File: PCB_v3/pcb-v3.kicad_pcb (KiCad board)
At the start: 2 copper layers, 6 parts, among them J1 Conn_02x20_Odd_Even, J2 Conn_01x07_Socket, J4 Screw_Terminal_01x02

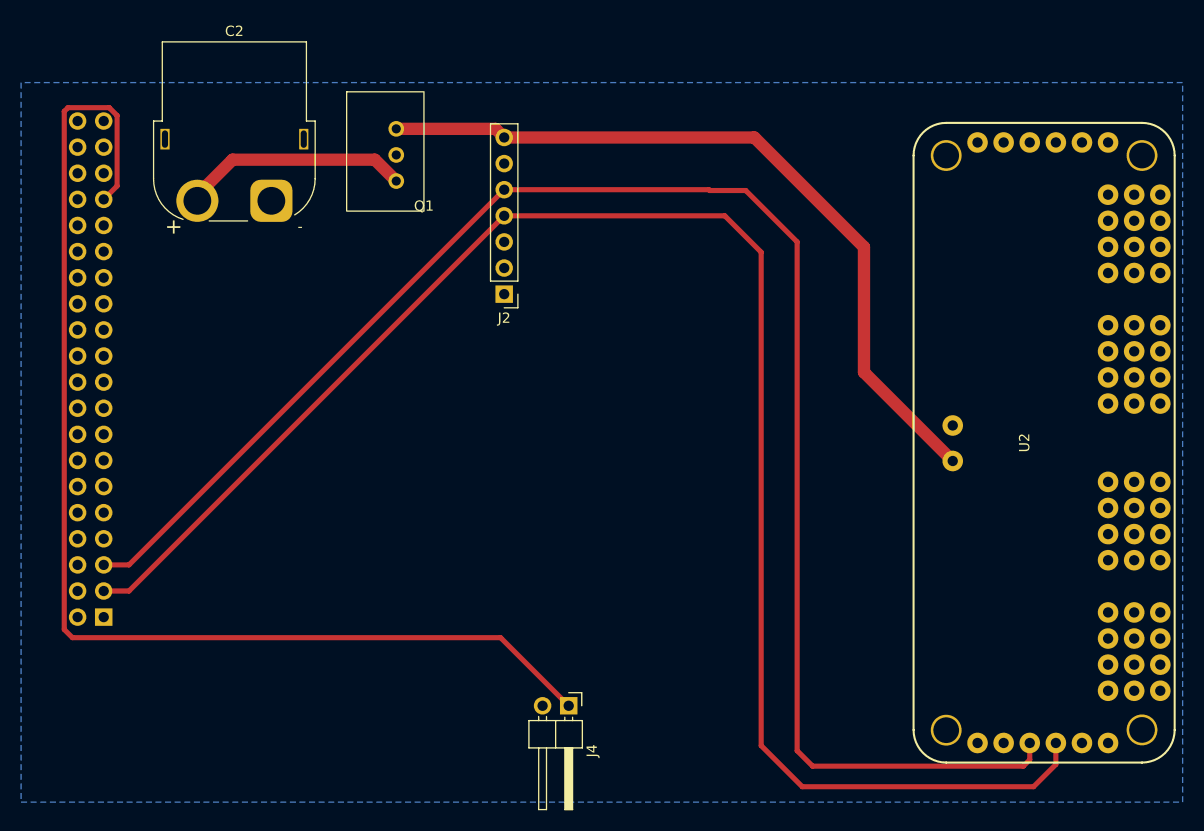
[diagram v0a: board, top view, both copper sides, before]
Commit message: completed board with labels included
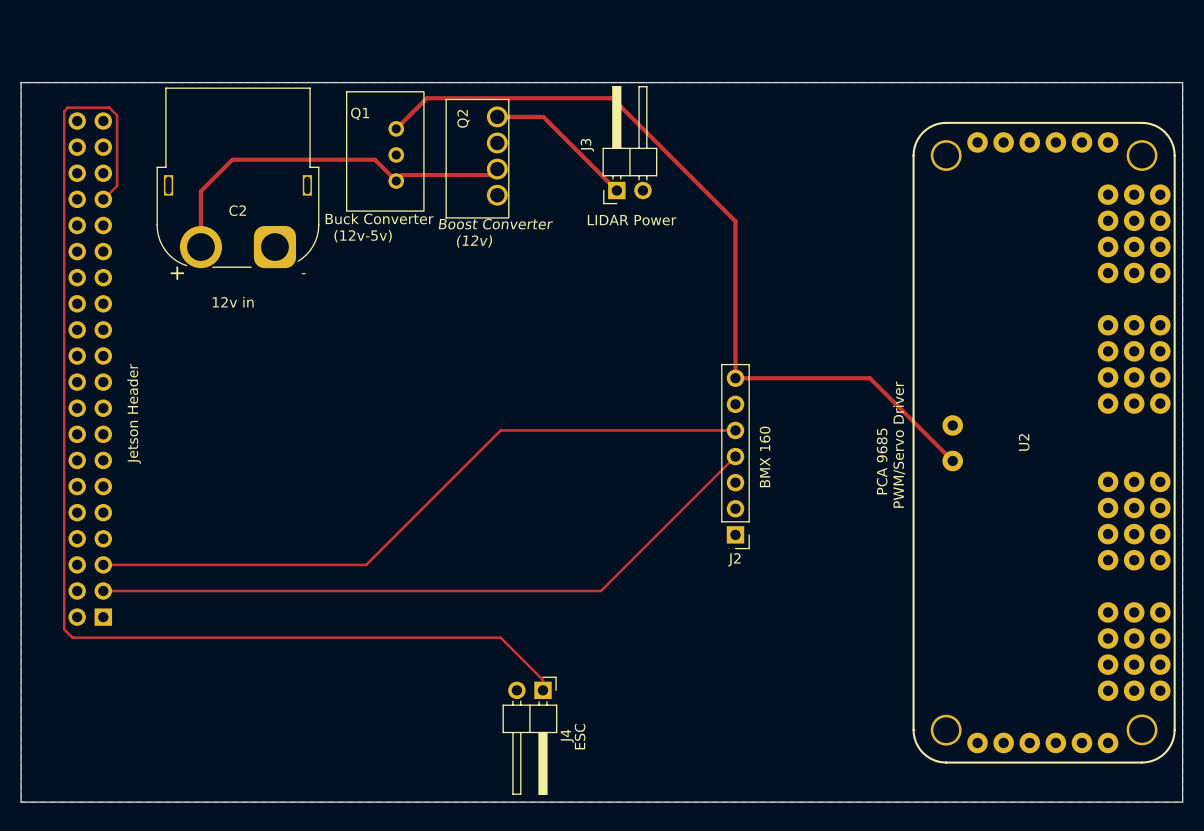
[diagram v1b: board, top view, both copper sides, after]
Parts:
- removed J1: Conn_02x20_Odd_Even, Connector_PinSocket_2.54mm:PinSocket_2x20_P2.54mm_Vertical
- added J3: Screw_Terminal_01x02, Connector_PinHeader_2.54mm:PinHeader_1x02_P2.54mm_Horizontal, F.Cu at (182.0, 37.5)
- added J5: Conn_02x20_Odd_Even, Connector_PinSocket_2.54mm:PinSocket_2x20_P2.54mm_Vertical, B.Cu at (132.0, 79.0)
- added Q2: ~, Cruz_Control_Footprints:CRE1S Boost Converter, F.Cu at (171.4, 40.2)
- moved J2 32.5 mm to (193.5, 71.0)
- moved C2 4.51 mm to (148.7, 43.0)
- moved J4 2.92 mm to (174.8, 86.1)
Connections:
- U2 pad 14: unconnected-(U2-PWM0-Pad6) -> GND
- U2 pad 6: GND -> unconnected-(U2-PWM0-Pad6)
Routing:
- net SDA: track 161.9 -> 66.9 mm
- net SCL: track 159.3 -> 66.9 mm
- net +12V: track 22.2 -> 36.9 mm
- net P.LIDAR: track 0.00 -> 14.6 mm
- net +5V: track 74.7 -> 78.9 mm
- net ESC: track 116.9 -> 114.3 mm
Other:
- board outline added: 113 x 70 mm
- board text added: "12v in"
- board text added: "BMX 160"
- board text added: "Boost Converter (12v)"
- board text added: "Buck Converter (12v-5v)"
- board text added: "ESC"
- board text added: "Jetson Header"
- board text added: "LIDAR Power"
- board text added: "PCA 9685 PWM/Servo Driver"

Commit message: updated PCB
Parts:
- added J1: Screw_Terminal_01x02, Connector_PinHeader_2.54mm:PinHeader_1x02_P2.54mm_Horizontal, F.Cu at (175.7, 37.5)
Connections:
- net P.LIDAR renamed STABLE_12V
- J5 pad 1: +3.3V -> (no net)
- J5 pad 14: (no net) -> GND
- J5 pad 17: +3.3V -> (no net)
- J5 pad 2: +5V -> (no net)
- J5 pad 20: (no net) -> GND
- J5 pad 25: (no net) -> GND
- J5 pad 30: (no net) -> GND
- J5 pad 34: (no net) -> GND
- J5 pad 4: +5V -> (no net)
- J5 pad 6: (no net) -> GND
- J5 pad 9: (no net) -> GND
- U2 pad 3: unconnected-(U2-A2-Pad3) -> SDA
- U2 pad 4: unconnected-(U2-A3-Pad4)_0 -> SCL
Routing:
- net SDA: track 66.9 -> 118.9 mm
- net SCL: track 66.9 -> 109.1 mm
- net STABLE_12V: track 14.6 -> 22.8 mm
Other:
- board text added: "Jetson Power"

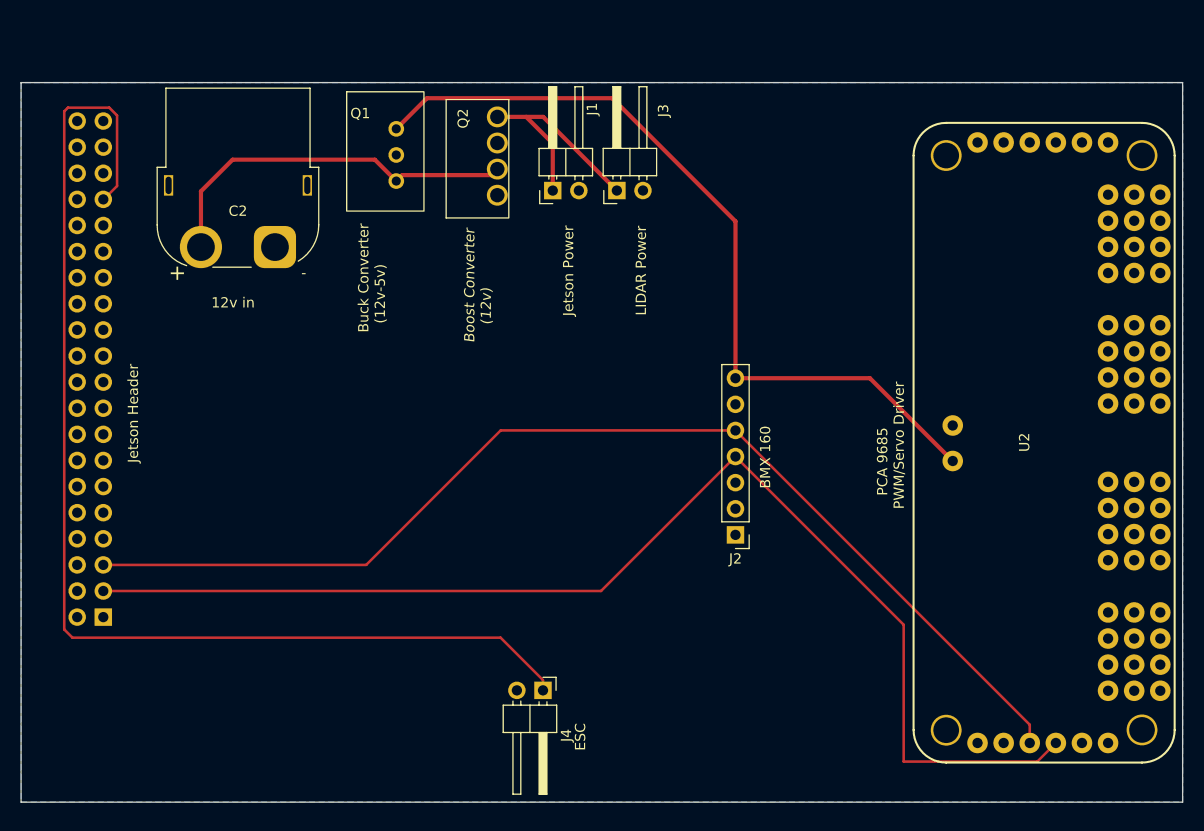
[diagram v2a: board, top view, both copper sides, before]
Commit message: added mounting holes to PCB
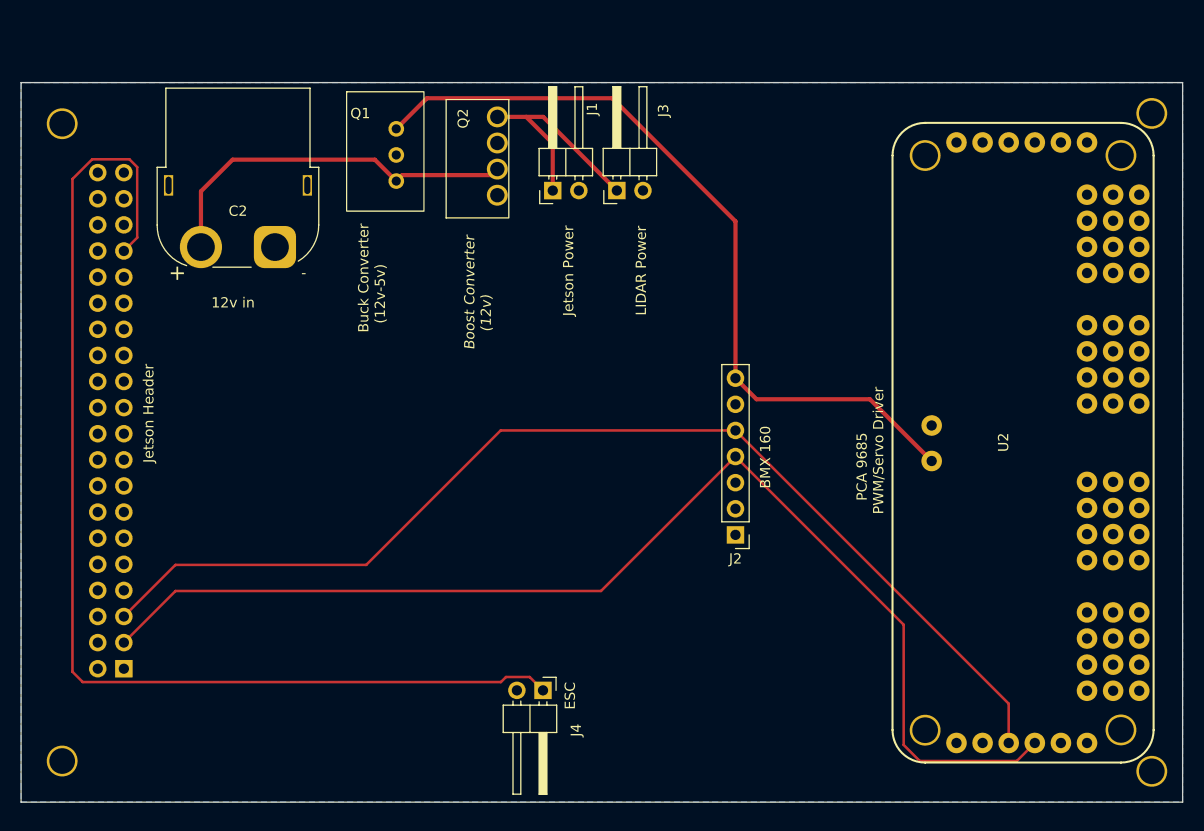
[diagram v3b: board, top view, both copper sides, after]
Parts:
- added ?: , , F.Cu at (234.0, 30.0)
- added ?: , , F.Cu at (128.0, 93.0)
- added ?: , , F.Cu at (128.0, 31.0)
- added ?: , , F.Cu at (234.0, 94.0)
- moved J5 5.40 mm to (134.0, 84.0)
- moved U2 2.05 mm to (231.0, 90.0)
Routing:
- net ESC: track 114.3 -> 111.0 mm
- net SDA: track 118.9 -> 116.0 mm
- net +5V: track 78.9 -> 76.9 mm
- net SCL: track 109.1 -> 108.4 mm

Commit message: Finishing touches
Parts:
- added C1: CP_Radial_D6.3mm_P2.50mm, Capacitor_THT:CP_Radial_D6.3mm_P2.50mm, F.Cu at (166.0, 81.0)
- added C2: CP_Radial_D6.3mm_P2.50mm, Capacitor_THT:CP_Radial_D6.3mm_P2.50mm, F.Cu at (181.0, 67.0)
- added C3: CP_Radial_D6.3mm_P2.50mm, Capacitor_THT:CP_Radial_D6.3mm_P2.50mm, F.Cu at (181.0, 55.0)
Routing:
- net SDA: track 116.0 -> 124.1 mm
- net SCL: track 108.4 -> 114.7 mm
- net ESC: track 111.0 -> 116.5 mm
